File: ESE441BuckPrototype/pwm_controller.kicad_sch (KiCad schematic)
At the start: 54 parts, among them J1 Header

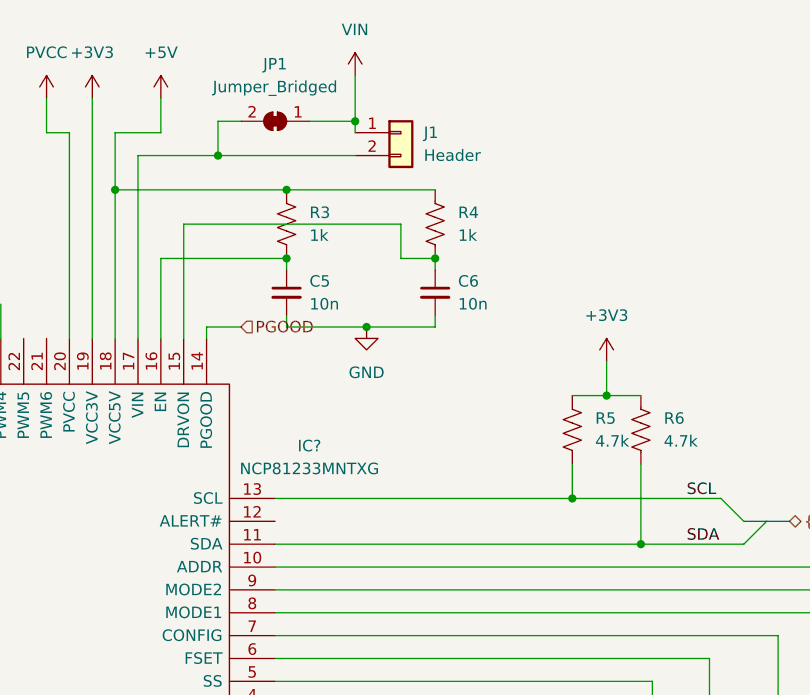
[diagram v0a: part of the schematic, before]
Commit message: Add ALERT# monitoring and fix input/output sheet pins
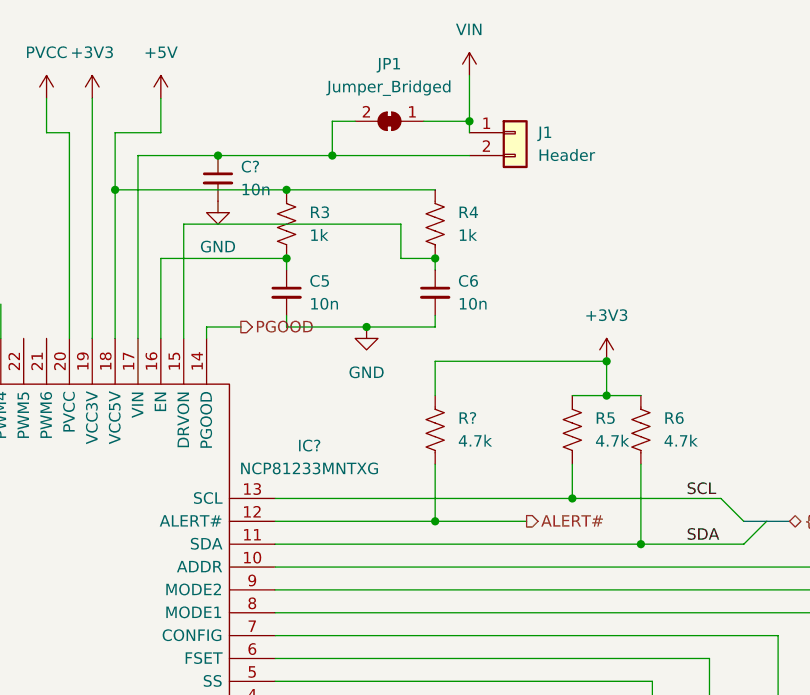
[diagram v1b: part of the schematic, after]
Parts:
- added C?: 10n, symbol Device:C_Small
- added R?: 4.7k, Resistor_SMD:R_0603_1608Metric, symbol Device:R_US
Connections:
- net +3V3: now also R?.1
- net GND: now also C?.2
- net at IC?.17 (VIN), J1.2 (Pin_2), JP1.2 (B): now also C?.1
- net ALERT#: now reaches IC?.12 (ALERT#)
- net ALERT#: now also R?.2
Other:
- moved on the sheet: J1, JP1
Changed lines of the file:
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@@
   (junction (at 55.88 140.97) (diameter 0) (color 0 0 0 0)
   )
+  (junction (at 177.8 53.34) (diameter 0) (color 0 0 0 0)
+  )
   (junction (at 175.26 107.95) (diameter 0) (color 0 0 0 0)
   )
@@
   (junction (at 106.68 148.59) (diameter 0) (color 0 0 0 0)
   )
+  (junction (at 147.32 30.48) (diameter 0) (color 0 0 0 0)
+  )
+  (junction (at 120.65 133.35) (diameter 0) (color 0 0 0 0)
+  )
+  (junction (at 158.75 71.12) (diameter 0) (color 0 0 0 0)
+  )
+  (junction (at 24.13 31.75) (diameter 0) (color 0 0 0 0)
+  )
   (junction (at 134.62 30.48) (diameter 0) (color 0 0 0 0)
   )
-  (junction (at 120.65 133.35) (diameter 0) (color 0 0 0 0)
-  )
-  (junction (at 24.13 31.75) (diameter 0) (color 0 0 0 0)
-  )
   (junction (at 52.07 140.97) (diameter 0) (color 0 0 0 0)
   )
@@
   (junction (at 196.85 107.95) (diameter 0) (color 0 0 0 0)
   )
-  (junction (at 149.86 26.67) (diameter 0) (color 0 0 0 0)
+  (junction (at 162.56 26.67) (diameter 0) (color 0 0 0 0)
   )
   (junction (at 139.7 132.08) (diameter 0) (color 0 0 0 0)
@@
     (stroke (width 0) (type default) (color 0 0 0 0))
   )
+  (wire (pts (xy 158.75 64.77) (xy 158.75 71.12))
+    (stroke (width 0) (type default) (color 0 0 0 0))
+  )
   (wire (pts (xy 106.68 139.7) (xy 106.68 148.59))
     (stroke (width 0) (type default) (color 0 0 0 0))
@@
     (stroke (width 0) (type default) (color 0 0 0 0))
   )
-  (wire (pts (xy 149.86 26.67) (xy 144.78 26.67))
+  (wire (pts (xy 162.56 26.67) (xy 157.48 26.67))
     (stroke (width 0) (type default) (color 0 0 0 0))
   )
@@
     (stroke (width 0) (type default) (color 0 0 0 0))
   )
+  (wire (pts (xy 134.62 30.48) (xy 147.32 30.48))
+    (stroke (width 0) (type default) (color 0 0 0 0))
+  )
   (wire (pts (xy 212.09 107.95) (xy 219.71 107.95))
     (stroke (width 0) (type default) (color 0 0 0 0))
   )
-  (wire (pts (xy 137.16 26.67) (xy 134.62 26.67))
+  (wire (pts (xy 149.86 26.67) (xy 147.32 26.67))
     (stroke (width 0) (type default) (color 0 0 0 0))
   )
@@
     (stroke (width 0) (type default) (color 0 0 0 0))
   )
+  (wire (pts (xy 140.97 71.12) (xy 158.75 71.12))
+    (stroke (width 0) (type default) (color 0 0 0 0))
+  )
   (wire (pts (xy 120.65 133.35) (xy 120.65 171.45))
     (stroke (width 0) (type default) (color 0 0 0 0))
@@
     (stroke (width 0) (type default) (color 0 0 0 0))
   )
-  (wire (pts (xy 149.86 21.59) (xy 149.86 26.67))
+  (wire (pts (xy 162.56 21.59) (xy 162.56 26.67))
     (stroke (width 0) (type default) (color 0 0 0 0))
   )
@@
     (stroke (width 0) (type default) (color 0 0 0 0))
   )
-  (wire (pts (xy 134.62 26.67) (xy 134.62 30.48))
+  (wire (pts (xy 147.32 26.67) (xy 147.32 30.48))
     (stroke (width 0) (type default) (color 0 0 0 0))
   )
@@
     (stroke (width 0) (type default) (color 0 0 0 0))
   )
+  (wire (pts (xy 158.75 71.12) (xy 168.91 71.12))
+    (stroke (width 0) (type default) (color 0 0 0 0))
+  )
   (wire (pts (xy 111.76 171.45) (xy 113.03 171.45))
     (stroke (width 0) (type default) (color 0 0 0 0))
@@
     (stroke (width 0) (type default) (color 0 0 0 0))
   )
+  (wire (pts (xy 158.75 53.34) (xy 158.75 57.15))
+    (stroke (width 0) (type default) (color 0 0 0 0))
+  )
   (wire (pts (xy 76.2 140.97) (xy 76.2 142.24))
     (stroke (width 0) (type default) (color 0 0 0 0))
@@
     (stroke (width 0) (type default) (color 0 0 0 0))
   )
+  (wire (pts (xy 158.75 53.34) (xy 177.8 53.34))
+    (stroke (width 0) (type default) (color 0 0 0 0))
+  )
   (wire (pts (xy 114.3 154.94) (xy 114.3 148.59))
     (stroke (width 0) (type default) (color 0 0 0 0))
@@
     (stroke (width 0) (type default) (color 0 0 0 0))
   )
-  (wire (pts (xy 134.62 30.48) (xy 149.86 30.48))
+  (wire (pts (xy 147.32 30.48) (xy 162.56 30.48))
     (stroke (width 0) (type default) (color 0 0 0 0))
   )
@@
     (stroke (width 0) (type default) (color 0 0 0 0))
   )
-  (wire (pts (xy 149.86 26.67) (xy 149.86 27.94))
+  (wire (pts (xy 162.56 26.67) (xy 162.56 27.94))
     (stroke (width 0) (type default) (color 0 0 0 0))
   )
@@
     (effects (font (size 1.27 1.27)) (justify right))
   )
-  (hierarchical_label "PGOOD" (shape input) (at 137.16 49.53 0)
+  (hierarchical_label "ALERT#" (shape output) (at 168.91 71.12 0)
+    (effects (font (size 1.27 1.27)) (justify left))
+  )
+  (hierarchical_label "PGOOD" (shape output) (at 137.16 49.53 0)
     (effects (font (size 1.27 1.27)) (justify left))
   )
@@
     (pin "2")
   )
+  (symbol (lib_id "Device:R_US") (at 158.75 60.96 0) (unit 1)
+    (in_bom yes) (on_board yes) (fields_autoplaced)
+    (property "Reference" "R?" (id 0) (at 161.29 59.6899 0)
+      (effects (font (size 1.27 1.27)) (justify left))
+    )
+    (property "Value" "4.7k" (id 1) (at 161.29 62.2299 0)
+      (effects (font (size 1.27 1.27)) (justify left))
+    )
+    (property "Footprint" "Resistor_SMD:R_0603_1608Metric" (id 2) (at 159.766 61.214 90)
+      (effects (font (size 1.27 1.27)) hide)
+    )
+    (property "Datasheet" "~" (id 3) (at 158.75 60.96 0)
+      (effects (font (size 1.27 1.27)) hide)
+    )
+    (pin "1")
+    (pin "2")
+  )
   (symbol (lib_id "Device:R_Potentiometer_Trim_US") (at 66.04 167.64 270) (unit 1)
     (in_bom yes) (on_board yes)
@@
     (pin "1")
   )
+  (symbol (lib_id "Device:C_Small") (at 134.62 33.02 0) (unit 1)
+    (in_bom yes) (on_board yes) (fields_autoplaced)
+    (property "Reference" "C?" (id 0) (at 137.16 31.7562 0)
+      (effects (font (size 1.27 1.27)) (justify left))
+    )
+    (property "Value" "10n" (id 1) (at 137.16 34.2962 0)
+      (effects (font (size 1.27 1.27)) (justify left))
+    )
+    (property "Footprint" "" (id 2) (at 134.62 33.02 0)
+      (effects (font (size 1.27 1.27)) hide)
+    )
+    (property "Datasheet" "~" (id 3) (at 134.62 33.02 0)
+      (effects (font (size 1.27 1.27)) hide)
+    )
+    (pin "1")
+    (pin "2")
+  )
   (symbol (lib_id "Device:C_Small") (at 212.09 137.16 0) (unit 1)
     (in_bom yes) (on_board yes) (fields_autoplaced)
@@
     (pin "1")
   )
+  (symbol (lib_id "power:GND") (at 134.62 35.56 0) (unit 1)
+    (in_bom yes) (on_board yes) (fields_autoplaced)
+    (property "Reference" "#PWR?" (id 0) (at 134.62 41.91 0)
+      (effects (font (size 1.27 1.27)) hide)
+    )
+    (property "Value" "GND" (id 1) (at 134.62 40.64 0))
+    (property "Footprint" "" (id 2) (at 134.62 35.56 0)
+      (effects (font (size 1.27 1.27)) hide)
+    )
+    (property "Datasheet" "" (id 3) (at 134.62 35.56 0)
+      (effects (font (size 1.27 1.27)) hide)
+    )
+    (pin "1")
+  )
   (symbol (lib_id "Device:C_Small") (at 59.69 132.08 90) (unit 1)
     (in_bom yes) (on_board yes)
@@
     (pin "2")
   )
-  (symbol (lib_id "Connector_Generic:Conn_01x02") (at 154.94 27.94 0) (unit 1)
-    (in_bom yes) (on_board yes) (fields_autoplaced)
-    (property "Reference" "J1" (id 0) (at 157.48 27.9399 0)
-      (effects (font (size 1.27 1.27)) (justify left))
-    )
-    (property "Value" "Header" (id 1) (at 157.48 30.4799 0)
-      (effects (font (size 1.27 1.27)) (justify left))
-    )
-    (property "Footprint" "" (id 2) (at 154.94 27.94 0)
-      (effects (font (size 1.27 1.27)) hide)
-    )
-    (property "Datasheet" "~" (id 3) (at 154.94 27.94 0)
-      (effects (font (size 1.27 1.27)) hide)
-    )
-    (pin "1")
-    (pin "2")
-  )
-  (symbol (lib_id "CustomPartsLibrary:VIN") (at 149.86 21.59 0) (unit 1)
-    (in_bom yes) (on_board yes) (fields_autoplaced)
-    (property "Reference" "#PWR?" (id 0) (at 149.86 25.4 0)
-      (effects (font (size 1.27 1.27)) hide)
-    )
-    (property "Value" "VIN" (id 1) (at 149.86 16.51 0))
-    (property "Footprint" "" (id 2) (at 149.86 21.59 0)
-      (effects (font (size 1.27 1.27)) hide)
-    )
-    (property "Datasheet" "" (id 3) (at 149.86 21.59 0)
+  (symbol (lib_id "Connector_Generic:Conn_01x02") (at 167.64 27.94 0) (unit 1)
+    (in_bom yes) (on_board yes) (fields_autoplaced)
+    (property "Reference" "J1" (id 0) (at 170.18 27.9399 0)
+      (effects (font (size 1.27 1.27)) (justify left))
+    )
+    (property "Value" "Header" (id 1) (at 170.18 30.4799 0)
+      (effects (font (size 1.27 1.27)) (justify left))
+    )
+    (property "Footprint" "" (id 2) (at 167.64 27.94 0)
+      (effects (font (size 1.27 1.27)) hide)
+    )
+    (property "Datasheet" "~" (id 3) (at 167.64 27.94 0)
+      (effects (font (size 1.27 1.27)) hide)
+    )
+    (pin "1")
+    (pin "2")
+  )
+  (symbol (lib_id "CustomPartsLibrary:VIN") (at 162.56 21.59 0) (unit 1)
+    (in_bom yes) (on_board yes) (fields_autoplaced)
+    (property "Reference" "#PWR?" (id 0) (at 162.56 25.4 0)
+      (effects (font (size 1.27 1.27)) hide)
+    )
+    (property "Value" "VIN" (id 1) (at 162.56 16.51 0))
+    (property "Footprint" "" (id 2) (at 162.56 21.59 0)
+      (effects (font (size 1.27 1.27)) hide)
+    )
+    (property "Datasheet" "" (id 3) (at 162.56 21.59 0)
       (effects (font (size 1.27 1.27)) hide)
     )
@@
     (pin "1")
   )
-  (symbol (lib_id "Jumper:SolderJumper_2_Bridged") (at 140.97 26.67 180) (unit 1)
-    (in_bom yes) (on_board yes) (fields_autoplaced)
-    (property "Reference" "JP1" (id 0) (at 140.97 20.32 0))
-    (property "Value" "Jumper_Bridged" (id 1) (at 140.97 22.86 0))
-    (property "Footprint" "" (id 2) (at 140.97 26.67 0)
-      (effects (font (size 1.27 1.27)) hide)
-    )
-    (property "Datasheet" "~" (id 3) (at 140.97 26.67 0)
-      (effects (font (size 1.27 1.27)) hide)
-    )
+  (symbol (lib_id "Jumper:SolderJumper_2_Bridged") (at 153.67 26.67 180) (unit 1)
+    (in_bom yes) (on_board yes) (fields_autoplaced)
+    (property "Reference" "JP1" (id 0) (at 153.67 20.32 0))
+    (property "Value" "Jumper_Bridged" (id 1) (at 153.67 22.86 0))
+    (property "Footprint" "" (id 2) (at 153.67 26.67 0)
+      (effects (font (size 1.27 1.27)) hide)
+    )
+    (property "Datasheet" "~" (id 3) (at 153.67 26.67 0)
+      (effects (font (size 1.27 1.27)) hide)
+    )

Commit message: Add optional LDO and annotations
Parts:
- gave numbers to parts that had none: 8
- renumbered Rdfb to Rdfb1, Rdrp to Rdrp1, Rx to Rx1
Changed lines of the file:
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@@
   (symbol (lib_id "power:VCC") (at 52.07 24.13 0) (unit 1)
     (in_bom yes) (on_board yes) (fields_autoplaced)
-    (property "Reference" "#PWR?" (id 0) (at 52.07 27.94 0)
+    (property "Reference" "#PWR0114" (id 0) (at 52.07 27.94 0)
       (effects (font (size 1.27 1.27)) hide)
     )
@@
   (symbol (lib_id "power:GND") (at 179.07 144.78 0) (unit 1)
     (in_bom yes) (on_board yes) (fields_autoplaced)
-    (property "Reference" "#PWR?" (id 0) (at 179.07 151.13 0)
+    (property "Reference" "#PWR0105" (id 0) (at 179.07 151.13 0)
       (effects (font (size 1.27 1.27)) hide)
     )
@@
   (symbol (lib_id "power:GND") (at 24.13 46.99 0) (unit 1)
     (in_bom yes) (on_board yes) (fields_autoplaced)
-    (property "Reference" "#PWR?" (id 0) (at 24.13 53.34 0)
+    (property "Reference" "#PWR0110" (id 0) (at 24.13 53.34 0)
       (effects (font (size 1.27 1.27)) hide)
     )
@@
   (symbol (lib_id "Device:R_US") (at 102.87 148.59 90) (mirror x) (unit 1)
     (in_bom yes) (on_board yes)
-    (property "Reference" "Rdfb" (id 0) (at 102.87 143.51 90))
+    (property "Reference" "Rdfb1" (id 0) (at 102.87 143.51 90))
     (property "Value" "10k" (id 1) (at 102.87 146.05 90))
     (property "Footprint" "Resistor_SMD:R_0603_1608Metric" (id 2) (at 103.124 149.606 90)
@@
   (symbol (lib_id "Device:R_US") (at 115.57 129.54 0) (mirror x) (unit 1)
     (in_bom yes) (on_board yes)
-    (property "Reference" "Rdrp" (id 0) (at 119.38 128.27 0))
+    (property "Reference" "Rdrp1" (id 0) (at 119.38 128.27 0))
     (property "Value" "1k" (id 1) (at 119.38 130.81 0))
     (property "Footprint" "Resistor_SMD:R_0603_1608Metric" (id 2) (at 116.586 129.286 90)
@@
   (symbol (lib_id "power:GND") (at 151.13 49.53 0) (unit 1)
     (in_bom yes) (on_board yes) (fields_autoplaced)
-    (property "Reference" "#PWR?" (id 0) (at 151.13 55.88 0)
+    (property "Reference" "#PWR0102" (id 0) (at 151.13 55.88 0)
       (effects (font (size 1.27 1.27)) hide)
     )
@@
   (symbol (lib_id "power:+1V0") (at 186.69 129.54 0) (unit 1)
     (in_bom yes) (on_board yes) (fields_autoplaced)
-    (property "Reference" "#PWR?" (id 0) (at 186.69 133.35 0)
+    (property "Reference" "#PWR0108" (id 0) (at 186.69 133.35 0)
       (effects (font (size 1.27 1.27)) hide)
     )
@@
   (symbol (lib_id "Device:R_US") (at 110.49 148.59 270) (mirror x) (unit 1)
     (in_bom yes) (on_board yes)
-    (property "Reference" "Rx" (id 0) (at 110.49 143.51 90))
+    (property "Reference" "Rx1" (id 0) (at 110.49 143.51 90))
     (property "Value" "6.25k" (id 1) (at 110.49 146.05 90))
     (property "Footprint" "Resistor_SMD:R_0603_1608Metric" (id 2) (at 110.236 147.574 90)
@@
   (symbol (lib_id "power:GND") (at 133.35 125.73 0) (unit 1)
     (in_bom yes) (on_board yes) (fields_autoplaced)
-    (property "Reference" "#PWR?" (id 0) (at 133.35 132.08 0)
+    (property "Reference" "#PWR0107" (id 0) (at 133.35 132.08 0)
       (effects (font (size 1.27 1.27)) hide)
     )
@@
   (symbol (lib_id "Device:R_US") (at 158.75 60.96 0) (unit 1)
     (in_bom yes) (on_board yes) (fields_autoplaced)
-    (property "Reference" "R?" (id 0) (at 161.29 59.6899 0)
+    (property "Reference" "R29" (id 0) (at 161.29 59.6899 0)
       (effects (font (size 1.27 1.27)) (justify left))
     )
@@
   (symbol (lib_id "power:GND") (at 67.31 132.08 90) (mirror x) (unit 1)
     (in_bom yes) (on_board yes) (fields_autoplaced)
-    (property "Reference" "#PWR?" (id 0) (at 73.66 132.08 0)
+    (property "Reference" "#PWR0119" (id 0) (at 73.66 132.08 0)
       (effects (font (size 1.27 1.27)) hide)
     )
@@
   (symbol (lib_id "Device:C_Small") (at 134.62 33.02 0) (unit 1)
     (in_bom yes) (on_board yes) (fields_autoplaced)
-    (property "Reference" "C?" (id 0) (at 137.16 31.7562 0)
+    (property "Reference" "C21" (id 0) (at 137.16 31.7562 0)
       (effects (font (size 1.27 1.27)) (justify left))
     )
@@
   (symbol (lib_id "Device:R_US") (at 68.58 72.39 0) (unit 1)
     (in_bom yes) (on_board yes) (fields_autoplaced)
-    (property "Reference" "R?" (id 0) (at 71.12 71.1199 0)
+    (property "Reference" "R28" (id 0) (at 71.12 71.1199 0)
       (effects (font (size 1.27 1.27)) (justify left))
     )
@@
   (symbol (lib_id "power:+5V") (at 128.27 24.13 0) (unit 1)
     (in_bom yes) (on_board yes) (fields_autoplaced)
-    (property "Reference" "#PWR?" (id 0) (at 128.27 27.94 0)
+    (property "Reference" "#PWR0118" (id 0) (at 128.27 27.94 0)
       (effects (font (size 1.27 1.27)) hide)
     )
@@
   (symbol (lib_id "power:+3V3") (at 177.8 53.34 0) (unit 1)
     (in_bom yes) (on_board yes) (fields_autoplaced)
-    (property "Reference" "#PWR?" (id 0) (at 177.8 57.15 0)
+    (property "Reference" "#PWR0104" (id 0) (at 177.8 57.15 0)
       (effects (font (size 1.27 1.27)) hide)
     )
@@
   (symbol (lib_id "power:GND") (at 68.58 76.2 0) (unit 1)
     (in_bom yes) (on_board yes) (fields_autoplaced)
-    (property "Reference" "#PWR?" (id 0) (at 68.58 82.55 0)
+    (property "Reference" "#PWR0120" (id 0) (at 68.58 82.55 0)
       (effects (font (size 1.27 1.27)) hide)
     )
@@
   (symbol (lib_id "power:GND") (at 134.62 35.56 0) (unit 1)
     (in_bom yes) (on_board yes) (fields_autoplaced)
-    (property "Reference" "#PWR?" (id 0) (at 134.62 41.91 0)
+    (property "Reference" "#PWR0101" (id 0) (at 134.62 41.91 0)
       (effects (font (size 1.27 1.27)) hide)
     )
@@
   (symbol (lib_id "Device:R_US") (at 68.58 64.77 0) (unit 1)
     (in_bom yes) (on_board yes) (fields_autoplaced)
-    (property "Reference" "R?" (id 0) (at 71.12 63.4999 0)
+    (property "Reference" "R22" (id 0) (at 71.12 63.4999 0)
       (effects (font (size 1.27 1.27)) (justify left))
     )
@@
   (symbol (lib_id "Device:C_Small") (at 125.73 171.45 90) (unit 1)
     (in_bom yes) (on_board yes)
-    (property "Reference" "C?" (id 0) (at 125.7363 175.26 90))
+    (property "Reference" "C20" (id 0) (at 125.7363 175.26 90))
     (property "Value" "1u" (id 1) (at 125.7363 177.8 90))
     (property "Footprint" "" (id 2) (at 125.73 171.45 0)
@@
   (symbol (lib_id "Device:C_Small") (at 118.11 166.37 0) (unit 1)
     (in_bom yes) (on_board yes)
-    (property "Reference" "C?" (id 0) (at 114.3 165.1062 0)
+    (property "Reference" "C19" (id 0) (at 114.3 165.1062 0)
       (effects (font (size 1.27 1.27)) (justify left))
     )
@@
   (symbol (lib_id "power:+3V3") (at 43.18 24.13 0) (unit 1)
     (in_bom yes) (on_board yes) (fields_autoplaced)
-    (property "Reference" "#PWR?" (id 0) (at 43.18 27.94 0)
+    (property "Reference" "#PWR0115" (id 0) (at 43.18 27.94 0)
       (effects (font (size 1.27 1.27)) hide)
     )
@@
   (symbol (lib_id "power:GND") (at 171.45 110.49 0) (unit 1)
     (in_bom yes) (on_board yes) (fields_autoplaced)
-    (property "Reference" "#PWR?" (id 0) (at 171.45 116.84 0)
+    (property "Reference" "#PWR0109" (id 0) (at 171.45 116.84 0)
       (effects (font (size 1.27 1.27)) hide)
     )
@@
   (symbol (lib_id "CustomPartsLibrary:VIN") (at 162.56 21.59 0) (unit 1)
     (in_bom yes) (on_board yes) (fields_autoplaced)
-    (property "Reference" "#PWR?" (id 0) (at 162.56 25.4 0)
+    (property "Reference" "#PWR0103" (id 0) (at 162.56 25.4 0)
       (effects (font (size 1.27 1.27)) hide)
     )
@@
   (symbol (lib_id "Device:C_Small") (at 115.57 171.45 270) (unit 1)
     (in_bom yes) (on_board yes)
-    (property "Reference" "C?" (id 0) (at 115.5636 175.26 90))
+    (property "Reference" "C18" (id 0) (at 115.5636 175.26 90))
     (property "Value" "10n" (id 1) (at 115.5636 177.8 90))
     (property "Footprint" "" (id 2) (at 115.57 171.45 0)
@@
   (symbol (lib_id "NCP81233MNTXG:NCP81233MNTXG") (at 140.97 99.06 180) (unit 1)
     (in_bom yes) (on_board yes) (fields_autoplaced)
-    (property "Reference" "IC?" (id 0) (at 144.78 62.7505 0))
+    (property "Reference" "IC1" (id 0) (at 144.78 62.7505 0))
     (property "Value" "NCP81233MNTXG" (id 1) (at 144.78 65.2905 0))
     (property "Footprint" "QFN40P600X600X100-53N" (id 2) (at 96.52 116.84 0)
@@
   (symbol (lib_id "CustomPartsLibrary:PVCC") (at 115.57 24.13 0) (unit 1)
     (in_bom yes) (on_board yes) (fields_autoplaced)
-    (property "Reference" "#PWR?" (id 0) (at 115.57 27.94 0)
+    (property "Reference" "#PWR0117" (id 0) (at 115.57 27.94 0)
       (effects (font (size 1.27 1.27)) hide)
     )
@@
   (symbol (lib_id "power:+3V3") (at 120.65 24.13 0) (unit 1)
     (in_bom yes) (on_board yes) (fields_autoplaced)
-    (property "Reference" "#PWR?" (id 0) (at 120.65 27.94 0)
+    (property "Reference" "#PWR0116" (id 0) (at 120.65 27.94 0)
       (effects (font (size 1.27 1.27)) hide)
     )
@@
   (symbol (lib_id "CustomPartsLibrary:PVCC") (at 24.13 24.13 0) (unit 1)
     (in_bom yes) (on_board yes) (fields_autoplaced)
-    (property "Reference" "#PWR?" (id 0) (at 24.13 27.94 0)
+    (property "Reference" "#PWR0112" (id 0) (at 24.13 27.94 0)
       (effects (font (size 1.27 1.27)) hide)
     )
@@
   (symbol (lib_id "power:GNDPWR") (at 186.69 144.78 0) (unit 1)
     (in_bom yes) (on_board yes) (fields_autoplaced)
-    (property "Reference" "#PWR?" (id 0) (at 186.69 149.86 0)
+    (property "Reference" "#PWR0106" (id 0) (at 186.69 149.86 0)
       (effects (font (size 1.27 1.27)) hide)
     )
@@
   (symbol (lib_id "power:+5V") (at 68.58 60.96 0) (unit 1)
     (in_bom yes) (on_board yes) (fields_autoplaced)
-    (property "Reference" "#PWR?" (id 0) (at 68.58 64.77 0)
+    (property "Reference" "#PWR0111" (id 0) (at 68.58 64.77 0)
       (effects (font (size 1.27 1.27)) hide)
     )
@@
   (symbol (lib_id "power:+5V") (at 34.29 24.13 0) (unit 1)
     (in_bom yes) (on_board yes) (fields_autoplaced)
-    (property "Reference" "#PWR?" (id 0) (at 34.29 27.94 0)
-      (effects (font (size 1.27 1.27)) hide)
-    )
+    (property "Reference" "#PWR0113" (id 0) (at 34.29 27.94 0)
+      (effects (font (size 1.27 1.27)) hide)
+    )
